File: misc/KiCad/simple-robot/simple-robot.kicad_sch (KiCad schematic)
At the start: 43 parts, among them J1 Conn_01x03_Pin, J2 Conn_01x03_Pin, J3 Conn_01x03_Pin, M1 Motor_DC, M2 Motor_DC, U1 Pico2

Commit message: schematic v2
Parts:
- added C9: 100nF_Ceramic, Capacitor_THT:C_Disc_D5.0mm_W2.5mm_P2.50mm, symbol PCM_SL_Capacitors:100nF_Ceramic
- added J4: Conn_01x03_Pin, Connector_PinHeader_2.54mm:PinHeader_1x03_P2.54mm_Vertical, symbol Connector:Conn_01x03_Pin
- added M3: Motor_Servo, symbol Motor:Motor_Servo
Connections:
- net GND: now also C9.2, J4.3 (Pin_3), M3.3 (-)
- net at C2.1, C5.2, C8.1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: now also C9.1, J4.2 (Pin_2), M3.2 (+)
- net at U1.7 (GPIO5): now also J4.1 (Pin_1), M3.1 (PWM)
- no-connect marks 17 -> 16

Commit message: update schematic and pcb
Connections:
- net at ENCB1.2 (Pin_2), EncoderB1.3 (PA), TP4.1 (Pin_1): now also U1.12 (GPIO9); no longer U1.11 (GPIO8)
- net at IMU1.8 (INT): now also U1.11 (GPIO8); no longer U1.12 (GPIO9)
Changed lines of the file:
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@@
+	(wire
+		(pts
+			(xy 78.74 124.46) (xy 83.82 124.46)
+		)
+		(stroke
+			(width 0)
+			(type default)
+		)
+	)
 	(wire
 		(pts
@@
 	(wire
 		(pts
-			(xy 73.66 55.88) (xy 73.66 124.46)
+			(xy 73.66 55.88) (xy 73.66 127)
 		)
 		(stroke
@@
 	(wire
 		(pts
-			(xy 78.74 162.56) (xy 78.74 127)
-		)
-		(stroke
-			(width 0)
-			(type default)
-		)
-	)
-	(wire
-		(pts
 			(xy 198.12 143.51) (xy 212.09 143.51)
 		)
@@
 	(wire
 		(pts
+			(xy 83.82 127) (xy 73.66 127)
+		)
+		(stroke
+			(width 0)
+			(type default)
+		)
+	)
+	(wire
+		(pts
 			(xy 130.81 139.7) (xy 119.38 139.7)
 		)
@@
 	(wire
 		(pts
+			(xy 78.74 124.46) (xy 78.74 162.56)
+		)
+		(stroke
+			(width 0)
+			(type default)
+		)
+	)
+	(wire
+		(pts
 			(xy 124.46 165.1) (xy 55.88 165.1)
 		)
@@
 	(wire
 		(pts
-			(xy 73.66 124.46) (xy 83.82 124.46)
-		)
-		(stroke
-			(width 0)
-			(type default)
-		)
-	)
-	(wire
-		(pts
 			(xy 77.47 30.48) (xy 118.11 30.48)
 		)
@@
 		)
 		(stroke
-			(width 0)
-			(type default)
-		)
-	)
-	(wire
-		(pts
-			(xy 78.74 127) (xy 83.82 127)
-		)
-		(stroke

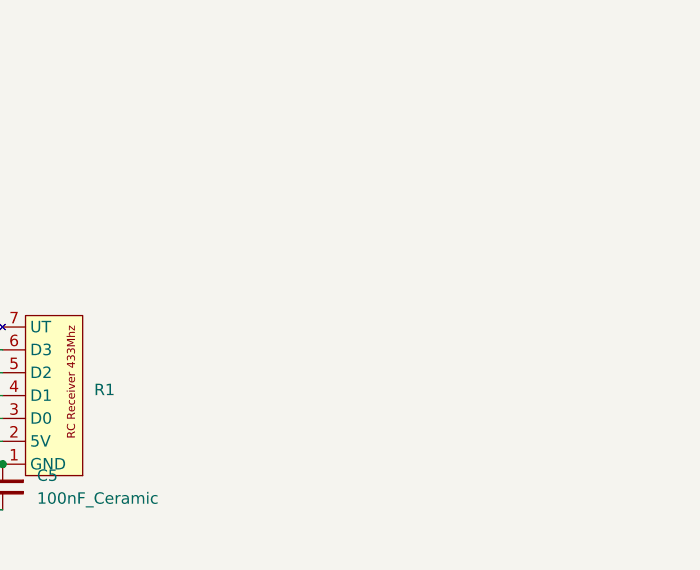
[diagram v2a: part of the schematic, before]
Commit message: update 3d models for hc-sr04 mount, update KiCad files, update schematic and PCB
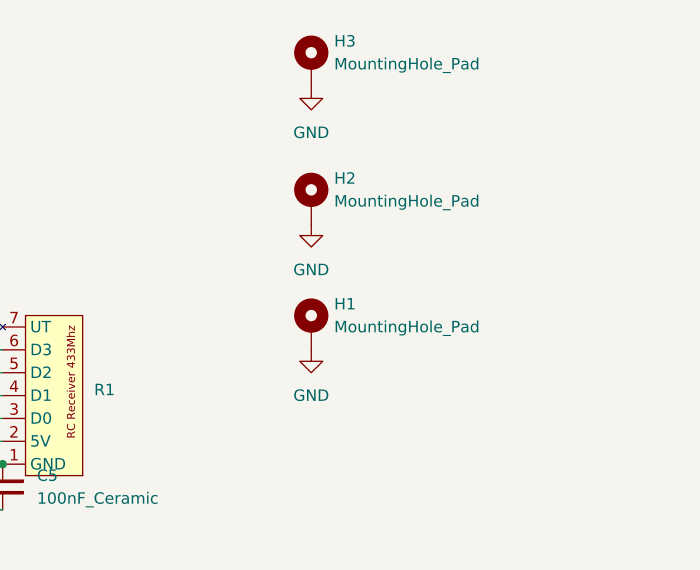
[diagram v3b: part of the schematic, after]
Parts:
- added H1, H2, H3: MountingHole_Pad, MountingHole:MountingHole_3.7mm_Pad_Via, symbol Mechanical:MountingHole_Pad
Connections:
- net GND: now also H1.1, H2.1, H3.1

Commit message: debugging & rewire
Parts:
- removed C2, C3: 47uF_25V, Capacitor_THT:CP_Radial_D5.0mm_P2.00mm, symbol PCM_SL_Capacitors:47uF_25V
- removed C7: 100nF_Ceramic, Capacitor_THT:C_Disc_D5.0mm_W2.5mm_P2.50mm, symbol PCM_SL_Capacitors:100nF_Ceramic
- removed D1, D2: 1N5817, Diode_THT:D_DO-41_SOD81_P10.16mm_Horizontal, symbol Diode:1N5817
- removed R4: 10k, Resistor_THT:R_Axial_DIN0207_L6.3mm_D2.5mm_P10.16mm_Horizontal, symbol PCM_SL_Resistors:10k
- removed R5: 20k, Resistor_THT:R_Axial_DIN0207_L6.3mm_D2.5mm_P10.16mm_Horizontal, symbol PCM_SL_Resistors:20k
- added C10, C11, C12, C13, C14, C15, C3: 100nF_Ceramic, Capacitor_THT:C_Disc_D5.0mm_W2.5mm_P2.50mm, symbol PCM_SL_Capacitors:100nF_Ceramic
- added C17, C2: 220uF_10V, Capacitor_THT:CP_Radial_D6.3mm_P2.50mm, symbol PCM_SL_Capacitors:220uF_10V
- added LS_2: ~, common-hobby-things:Level shifter 4 bi-dir, symbol common-hobby-things:level-shifter
- added TPGND1, TPGND2: Conn_01x01_Pin, symbol Connector:Conn_01x01_Pin
- renumbered J2 to DBG1, J3 to IRL1, J1 to IRR1, IR_Proximity_Sensor2 to IR_Sensor_Left1, IR_Proximity_Sensor1 to IR_Sensor_Right1, M1 to MA1, M2 to MB1, J4 to SERVO1, TP3 to TPENCA1, TP4 to TPENCB1, TP1 to TPSCL1, TP2 to TPSDA1
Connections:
- net GND: now also C4.2, C5.2, U1.13 (GND), U1.28 (GND), U1.8 (GND), C10.2, C11.1, C12.1, C13.2, C14.2, C15.2, C17.2, C2.2, C3.2, LS_2.10 (GND), LS_2.4 (GND), TPGND1.1 (Pin_1), TPGND2.1 (Pin_1); no longer C4.1, C5.1, U1.42 (GND)
- net at ENCB1.2 (Pin_2), EncoderB1.3 (PA), TPENCB1.1 (Pin_1): now also LS_2.7 (HV1); no longer U1.12 (GPIO9)
- net at C6.2, IMU1.1 (VCC), IRL1.2 (Pin_2)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: now also C4.1, C8.1, C14.1, C15.1, LS_2.3 (LV); no longer C4.2
- net at IRL1.1 (Pin_1), IR_Sensor_Left1.3 (OUT): now also U1.9 (GPIO6)
- net at C9.1, ENCA1.3 (Pin_3), ENCB1.3 (Pin_3)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: now also C5.1, C10.1, C11.2, C12.2, C13.1, C17.1, C3.1, LS_2.9 (HV); no longer C5.2, C8.1
- net at C1.1, MD1.7 (VMOT), S6V1.3 (VOUT): now also C2.1
- net at U1.31 (GPIO26_ADC0): now also IRR1.1 (Pin_1), IR_Sensor_Right1.3 (OUT)
- net at U1.19 (GPIO14): now also LS_2.5 (LV3)
- net at MD1.3 (A01), MOTA1.1 (Pin_1): now also MA1.1 (+); no longer MB1.1 (+)
- net at MD1.4 (A02), MOTA1.2 (Pin_2): now also MA1.2 (-); no longer MB1.2 (-)
- net at R1.3 (D0): now also LS_1.12 (HV4); no longer LS_1.7 (HV1)
- net at R1.4 (D1): now also LS_1.11 (HV3); no longer LS_1.8 (HV2)
- net at R1.5 (D2): now also LS_1.8 (HV2); no longer LS_1.11 (HV3)
- net at R1.6 (D3): now also LS_1.7 (HV1); no longer LS_1.12 (HV4)
- net at ENCA1.2 (Pin_2), EncoderA1.3 (PA), TPENCA1.1 (Pin_1): now also LS_2.8 (HV2); no longer U1.10 (GPIO7)
- net at LS_1.5 (LV3): now also U1.21 (GPIO16); no longer U1.14 (GPIO10)
- net at U1.15 (GPIO11): now also LS_1.2 (LV2); no longer LS_1.6 (LV4)
- net at HC-SR04-1.2 (TRIG), HC-SRo4.2 (Pin_2): now also LS_2.12 (HV4); no longer U1.20 (GPIO15)
- net at LS_1.1 (LV1): now also U1.22 (GPIO17); no longer U1.21 (GPIO16)
- net at HC-SR04-1.3 (ECHO), HC-SRo4.3 (Pin_3): now also LS_2.11 (HV3)
- new net: MB1.2 (-), MD1.5 (B02), MOTB1.2 (Pin_2)
- new net: MB1.1 (+), MD1.6 (B01), MOTB1.1 (Pin_1)
- new net: LS_2.1 (LV1), U1.12 (GPIO9)
- new net: LS_2.2 (LV2), U1.10 (GPIO7)
- new net: LS_2.6 (LV4), U1.20 (GPIO15)
- new net: LS_1.6 (LV4), U1.14 (GPIO10)
- no-connect marks 16 -> 13
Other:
- moved on the sheet: BATT1, C1, C4, C5, C6, C9, D3, DBG1, ENCA1, ENCB1, EncoderA1, EncoderB1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

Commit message: Update KiCad project files and remove unnecessary autosave and lock files
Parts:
- TPGND1, TPGND2: footprint (none) -> Connector_PinHeader_2.54mm:PinHeader_1x01_P2.54mm_Vertical
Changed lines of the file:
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@@
 			)
 		)
-		(property "Footprint" ""
+		(property "Footprint" "Connector_PinHeader_2.54mm:PinHeader_1x01_P2.54mm_Vertical"
 			(at 267.97 92.71 0)
 			(effects
@@
 			)
 		)
-		(property "Footprint" ""
+		(property "Footprint" "Connector_PinHeader_2.54mm:PinHeader_1x01_P2.54mm_Vertical"
 			(at 267.97 82.55 0)
 			(effects

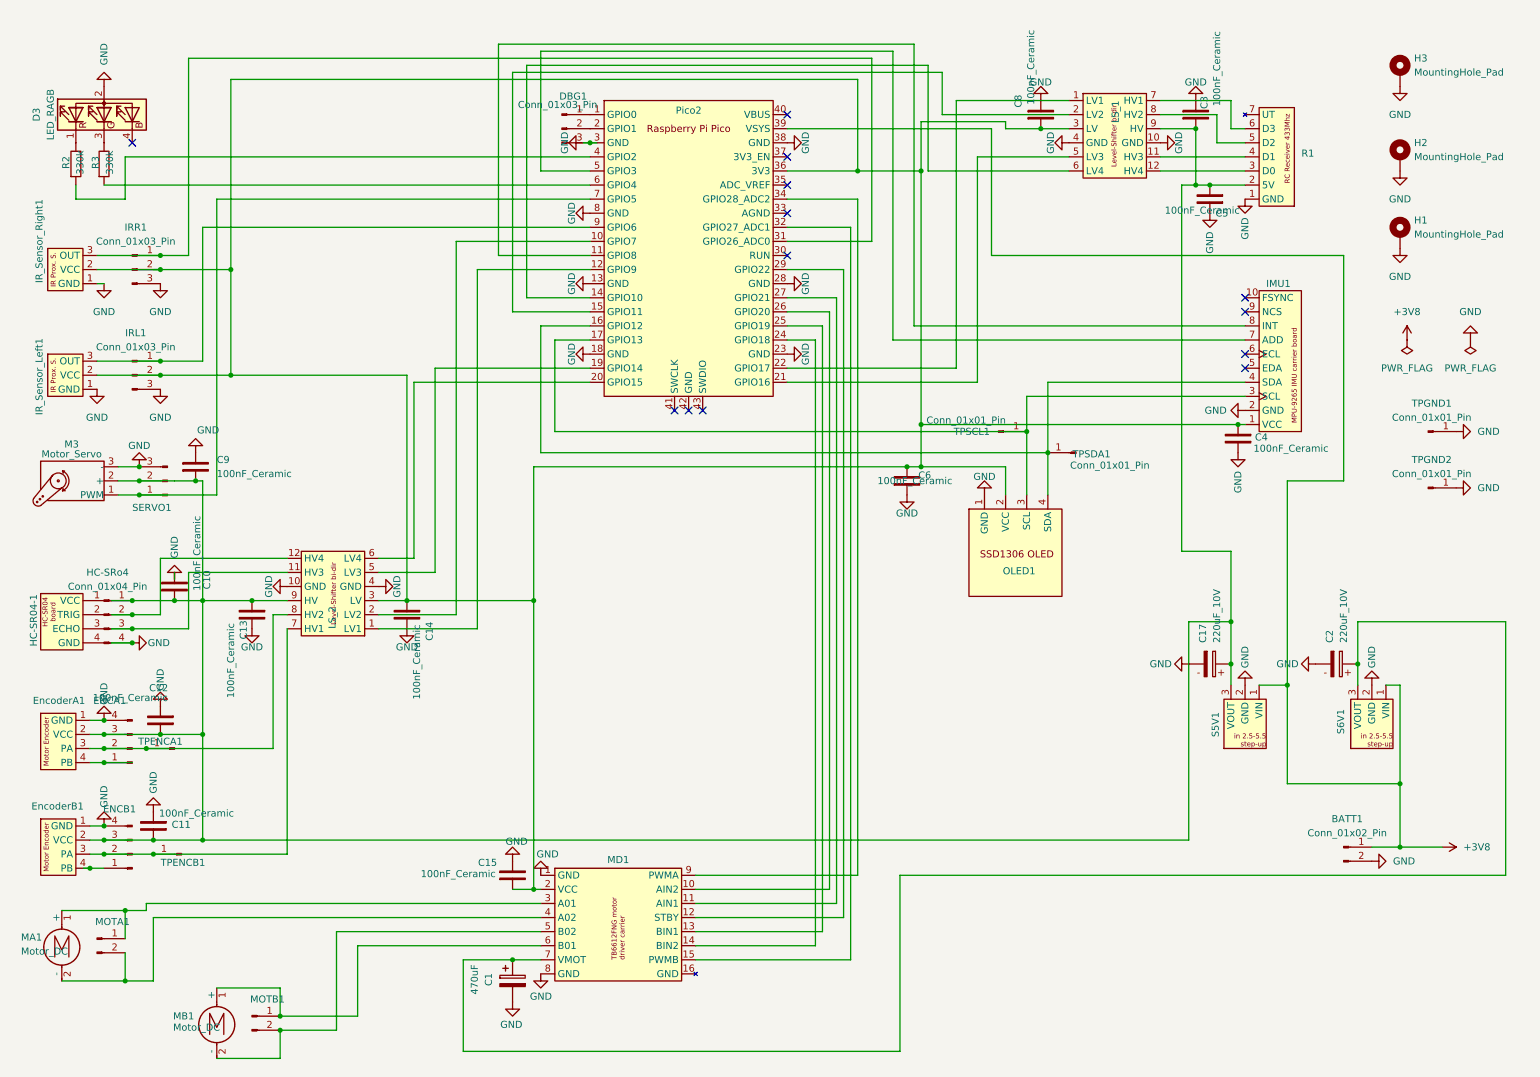
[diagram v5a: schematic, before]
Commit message: Dev into main (#18)
* Port expander and pin redistribution (#11)

* isolate few components to start with, comment the rest. Introduce new
motor driver without tb6612fng driver, also use a new port expander for
this.

* Add flash-backed calibration storage

Add sequential-storage and embedded-storage-async dependencies and use
the async Flash API. Reserve the last 8KB of flash in memory.x and
expose a FLASH_STORAGE region. Add src/task/flash_storage.rs which
implements a flash storage task, commands, and serialization for motor
and IMU calibration data. Remove the encoder_read task and update task
module, motor_driver docs, and main imports accordingly

* Include dev branch in CI workflow

* Fix PR review comments: correct type usage, add div-by-zero protection, fix memory.x comment

- Fixed incorrect type imports in drive.rs: use Track and Motor instead of MotorDriver and MotorSelection
- Updated all motor control calls to use correct Track enum (Left/Right) instead of incorrectly using Left for both sides
- Simplified MotorState methods to use SetTrack commands for controlling entire tracks
- Added division by zero protection in motor calibration routine (3 locations)
- Fixed memory.x comment to correctly state 8KB (two 4KB sectors) allocation
- Updated CI workflow to include dev branch for push and PR triggers

* Group crate::task imports and fix ordering

* Fix clippy warnings for CI

- Rename FlashCommand variants to remove common 'Calibration' postfix
- Derive Default for CalibrationData instead of manual impl
- Use unsigned_abs() instead of abs() as u8 cast
- Rename PortExpanderCommand variants to remove common 'Set' prefix
- Collapse nested if statements for button state checking
- Use is_err() instead of redundant pattern matching
- Update all usage sites and documentation to match renamed variants

* Drive straight (#12)

* Refactor flash storage and init wiring

Use Signal to return motor and IMU calibration data and add
CalibrationKind/CalibrationDataKind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
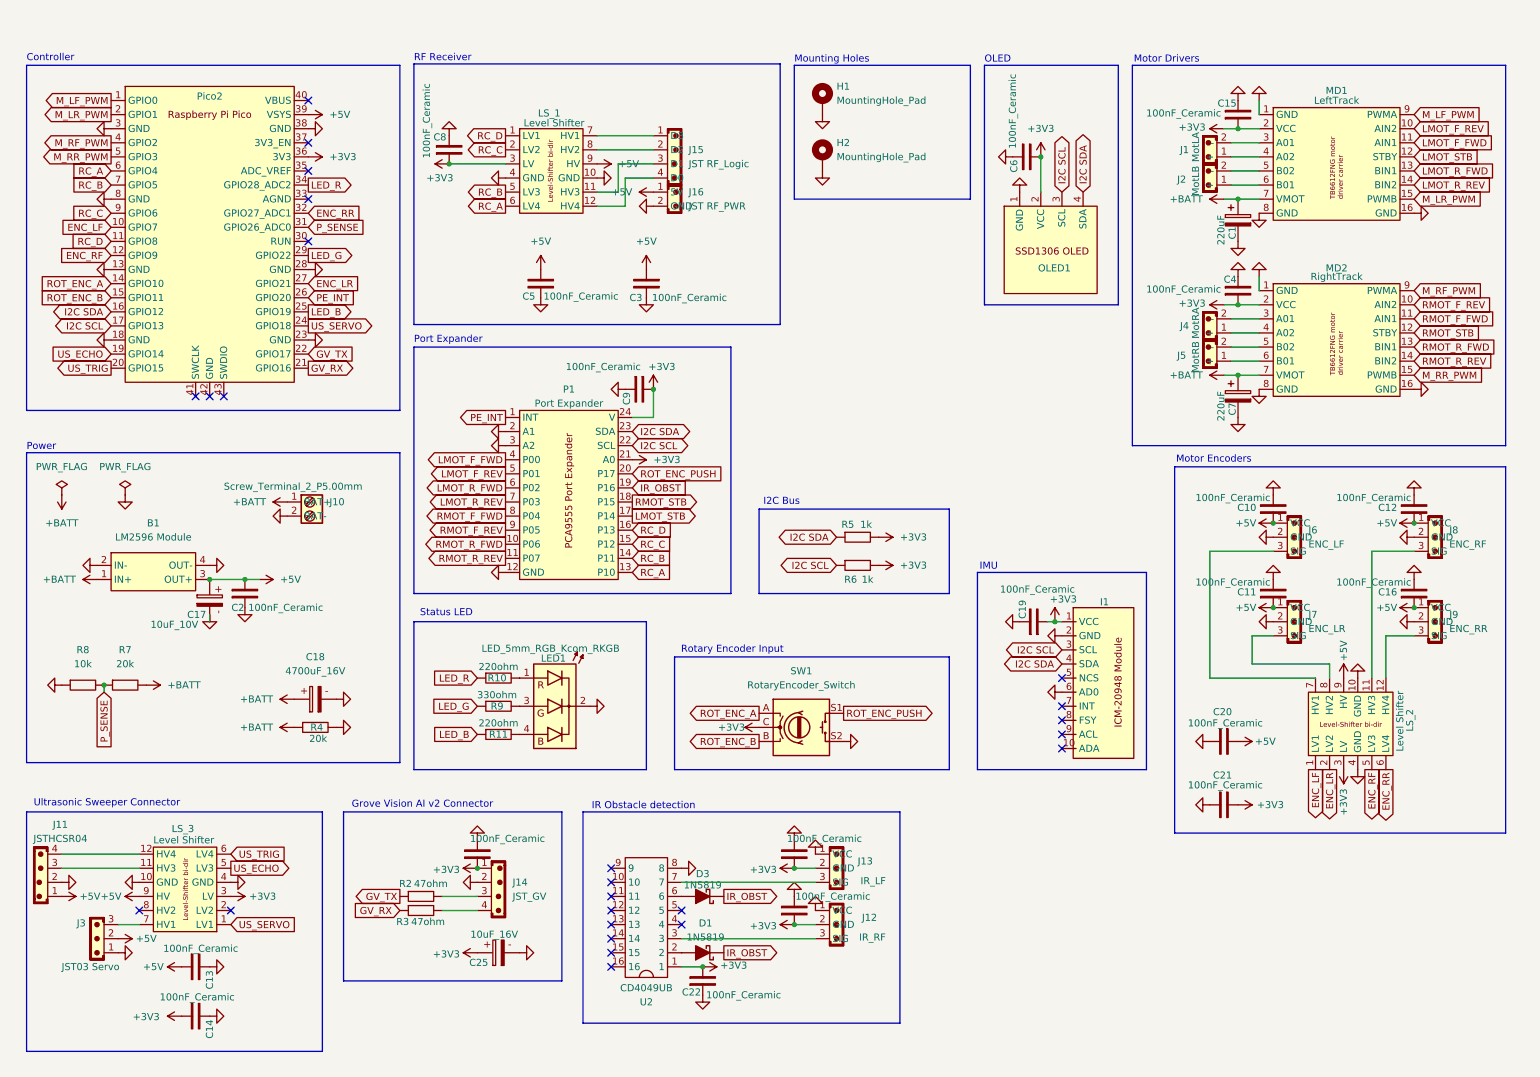
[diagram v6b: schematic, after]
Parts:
- removed BATT1: Conn_01x02_Pin, Connector_PinHeader_2.54mm:PinHeader_1x02_P2.54mm_Vertical, symbol Connector:Conn_01x02_Pin
- removed C2: 220uF_10V, Capacitor_THT:CP_Radial_D6.3mm_P2.50mm, symbol PCM_SL_Capacitors:220uF_10V
- removed D3: LED_RAGB, common-hobby-things:LED RAGB, symbol Device:LED_RAGB
- removed DBG1, IRL1, IRR1, SERVO1: Conn_01x03_Pin, Connector_PinHeader_2.54mm:PinHeader_1x03_P2.54mm_Vertical, symbol Connector:Conn_01x03_Pin
- removed ENCA1, ENCB1, HC-SRo4: Conn_01x04_Pin, Connector_PinHeader_2.54mm:PinHeader_1x04_P2.54mm_Vertical, symbol Connector:Conn_01x04_Pin
- removed EncoderA1, EncoderB1: ~, symbol common-hobby-things:Hall-effect_encoder
- removed H3: MountingHole_Pad, MountingHole:MountingHole_3.7mm_Pad_Via, symbol Mechanical:MountingHole_Pad
- removed HC-SR04-1: ~, symbol common-hobby-things:HC-SR04
- removed IMU1: ~, common-hobby-things:MPU 9265 IMU carrier board, symbol common-hobby-things:GY-9250_9-Axis
- removed IR_Sensor_Left1, IR_Sensor_Right1: ~, symbol common-hobby-things:IR_Proximity_Sensor
- removed M3: Motor_Servo, symbol Motor:Motor_Servo
- removed MA1, MB1: Motor_DC, symbol Motor:Motor_DC
- removed MOTA1, MOTB1: ~, Connector_PinHeader_2.54mm:PinHeader_1x02_P2.54mm_Vertical, symbol Connector:Conn_01x02_Pin
- removed R1: ~, common-hobby-things:433Mhz RC Receiver, symbol common-hobby-things:RC_Receiver
- removed R2, R3: 330k, Resistor_THT:R_Axial_DIN0207_L6.3mm_D2.5mm_P10.16mm_Horizontal, symbol PCM_SL_Resistors:330k
- removed S5V1: ~, common-hobby-things:Pololu step-up converter 2.5-5.5V in 5V out, symbol common-hobby-things:step-up-converter_5V
- removed S6V1: ~, common-hobby-things:Pololu step-up converter 2.5-5.5V in 6V out, symbol common-hobby-things:step-up-converter_6V
- removed TPENCA1, TPENCB1, TPGND1, TPGND2, TPSCL1, TPSDA1: Conn_01x01_Pin, Connector_PinHeader_2.54mm:PinHeader_1x01_P2.54mm_Vertical, symbol Connector:Conn_01x01_Pin
- added B1: LM2596 Module, common-hobby-things:LM2596_Module, symbol common-hobby-things:LM2596_Module
- added C16, C19, C2, C20, C21, C22, C23, C24, C26: 100nF_Ceramic, Capacitor_THT:C_Disc_D5.0mm_W2.5mm_P2.50mm, symbol PCM_SL_Capacitors:100nF_Ceramic
- added C18: 4700uF_16V, Capacitor_THT:CP_Radial_D16.0mm_P7.50mm, symbol PCM_SL_Capacitors:4700uF_16V
- added C25: 10uF_16V, Capacitor_THT:CP_Radial_D5.0mm_P2.00mm, symbol PCM_SL_Capacitors:10uF_16V
- added C7: 220uF, Capacitor_THT:CP_Radial_D6.3mm_P2.50mm, symbol Device:C_Polarized
- added D1, D3: 1N5819, PCM_Diode_THT_AKL:D_DO-41_SOD81_P7.62mm_Horizontal, symbol PCM_Diode_Schottky_AKL:1N5819
- added I1: ~, common-hobby-things:ICM-20948-module, symbol common-hobby-things:ICM-20948-module
- added J1: MotLA, Connector_JST:JST_PH_B2B-PH-K_1x02_P2.00mm_Vertical, symbol PCM_SL_Connectors:JST_02
- added J10: Screw_Terminal_2_P5.00mm, TerminalBlock_Phoenix:TerminalBlock_Phoenix_PT-1,5-2-5.0-H_1x02_P5.00mm_Horizontal, symbol PCM_SL_Screw_Terminal:Screw_Terminal_2_P5.00mm
- added J11: JSTHCSR04, Connector_JST:JST_EH_B4B-EH-A_1x04_P2.50mm_Vertical, symbol PCM_SL_Connectors:JST_04
- added J12: IR_RF, Connector_JST:JST_PH_B3B-PH-K_1x03_P2.00mm_Vertical, symbol PCM_SL_Connectors:JST_03
- added J13: IR_LF, Connector_JST:JST_PH_B3B-PH-K_1x03_P2.00mm_Vertical, symbol PCM_SL_Connectors:JST_03
- added J14: JST_GV, Connector_JST:JST_EH_B4B-EH-A_1x04_P2.50mm_Vertical, symbol PCM_SL_Connectors:JST_04
- added J15: JST RF_Logic, Connector_JST:JST_EH_B4B-EH-A_1x04_P2.50mm_Vertical, symbol PCM_SL_Connectors:JST_04
- added J16: JST RF_PWR, Connector_JST:JST_EH_B2B-EH-A_1x02_P2.50mm_Vertical, symbol PCM_SL_Connectors:JST_02
- added J2: MotLB, Connector_JST:JST_PH_B2B-PH-K_1x02_P2.00mm_Vertical, symbol PCM_SL_Connectors:JST_02
- added J3: JST03 Servo, Connector_JST:JST_EH_B3B-EH-A_1x03_P2.50mm_Vertical, symbol PCM_SL_Connectors:JST_03
- added J4: MotRA, Connector_JST:JST_PH_B2B-PH-K_1x02_P2.00mm_Vertical, symbol PCM_SL_Connectors:JST_02
- added J5: MotRB, Connector_JST:JST_PH_B2B-PH-K_1x02_P2.00mm_Vertical, symbol PCM_SL_Connectors:JST_02
- added J6: ENC_LF, Connector_JST:JST_PH_B3B-PH-K_1x03_P2.00mm_Vertical, symbol PCM_SL_Connectors:JST_03
- added J7: ENC_LR, Connector_JST:JST_PH_B3B-PH-K_1x03_P2.00mm_Vertical, symbol PCM_SL_Connectors:JST_03
- added J8: ENC_RF, Connector_JST:JST_PH_B3B-PH-K_1x03_P2.00mm_Vertical, symbol PCM_SL_Connectors:JST_03
- added J9: ENC_RR, Connector_JST:JST_PH_B3B-PH-K_1x03_P2.00mm_Vertical, symbol PCM_SL_Connectors:JST_03
- added LED1: LED_5mm_RGB_Kcom_RKGB, PCM_LED_THT_AKL:LED_D5.0mm-4_RGB_Wide_Pins, symbol PCM_LED_AKL:LED_5mm_RGB_Kcom_RKGB
- added LS_3: Level Shifter, common-hobby-things:Level shifter 4 bi-dir, symbol common-hobby-things:level-shifter
- added MD2: RightTrack, common-hobby-things:TB6612FNG motor driver carrier, symbol common-hobby-things:TB6612FNG motor driver carrier
- added P1: Port Expander, common-hobby-things:PCA9555 Port Expander, symbol common-hobby-things:PCA9555
- added R10, R11: 220ohm, Resistor_THT:R_Axial_DIN0207_L6.3mm_D2.5mm_P10.16mm_Horizontal, symbol PCM_SL_Resistors:220ohm
- added R2, R3: 47ohm, Resistor_THT:R_Axial_DIN0207_L6.3mm_D2.5mm_P10.16mm_Horizontal, symbol PCM_SL_Resistors:47ohm
- added R4, R7: 20k, Resistor_THT:R_Axial_DIN0207_L6.3mm_D2.5mm_P10.16mm_Horizontal, symbol PCM_SL_Resistors:20k
- added R5, R6: 1k, Resistor_THT:R_Axial_DIN0207_L6.3mm_D2.5mm_P10.16mm_Horizontal, symbol PCM_SL_Resistors:1k
- added R8: 10k, Resistor_THT:R_Axial_DIN0207_L6.3mm_D2.5mm_P10.16mm_Horizontal, symbol PCM_SL_Resistors:10k
- added R9: 330ohm, Resistor_THT:R_Axial_DIN0207_L6.3mm_D2.5mm_P10.16mm_Horizontal, symbol PCM_SL_Resistors:330ohm
- added SW1: RotaryEncoder_Switch, Rotary_Encoder:RotaryEncoder_Alps_EC11E-Switch_Vertical_H20mm, symbol Device:RotaryEncoder_Switch
- added U2: CD4049UB, Package_DIP:DIP-16_W7.62mm_LongPads, symbol PCM_SL_Devices:IC_DIP_16
- C1: value 470uF -> 220uF
- C17: value 220uF_10V -> 10uF_10V
- LS_1, LS_2: value ~ -> Level Shifter
- MD1: value ~ -> LeftTrack
- U1: footprint MCU_RaspberryPi_and_Boards:RPi_Pico_SMD_TH -> PCM_SL_Development_Boards:raspberry_pi_pico_THT
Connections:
- net +3V8 is gone; now on net +5V: U1.39 (VSYS)
- net GND: now also C11.2, C12.2, C9.1, MD1.16 (GND), B1.2 (IN-), B1.4 (OUT-), C16.2, C18.2, C19.2, C2.1, C20.1, C21.1, C22.1, C23.2, C24.2, C25.2, C26.2, C7.2, I1.2 (GND), I1.6 (AD0), J10.2 (BAT-), J11.2, J12.1 (VCC), J13.1 (VCC), J14.2, J16.2 (GND), J3.1, J6.2 (GND), J7.2 (GND), J8.2 (GND), J9.2 (GND), LED1.2 (A), LS_3.10 (GND), LS_3.4 (GND), MD2.1 (GND), MD2.16 (GND), MD2.8 (GND), P1.12 (GND), P1.2 (A1), P1.3 (A2), R4.2, R8.1, SW1.S2, U2.8; no longer C11.1, C12.1, C9.2
- net at LS_2.7 (HV1): now also J6.3 (SIG)
- net +3V3: now reaches C14.1, C15.1, C4.1, C6.2, C8.1, LS_1.3 (LV), LS_2.3 (LV), MD1.2 (VCC), OLED1.2 (VCC), U1.36 (3V3)
- net +3V3: now also C9.2, C19.1, C21.2, C22.2, C23.1, C24.1, C25.1, C26.1, I1.1 (VCC), J12.2 (GND), J13.2 (GND), J14.1, LS_3.3 (LV), MD2.2 (VCC), P1.21 (A0), P1.24 (V), R5.2, R6.2, SW1.C, U2.1
- net RC_C: now reaches U1.9 (GPIO6)
- net RC_C: now also LS_1.2 (LV2), P1.15 (P12)
- net +5V: now reaches C10.1, C13.1, C17.1, C3.1, C5.1, LS_1.9 (HV), LS_2.9 (HV)
- net +5V: now also C11.1, C12.1, B1.3 (OUT+), C16.1, C2.2, C20.2, J11.1, J16.1 (5V), J3.2, J6.1 (VCC), J7.1 (VCC), J8.1 (VCC), J9.1 (VCC), LS_3.9 (HV); no longer C11.2, C12.2, C9.1
- net RC_B: now reaches U1.7 (GPIO5)
- net RC_B: now also LS_1.5 (LV3), P1.14 (P11)
- net M_RF_PWM: now reaches U1.4 (GPIO2)
- net M_RF_PWM: now also MD2.9 (PWMA)
- net I2C SDA: now reaches OLED1.4 (SDA), U1.16 (GPIO12)
- net I2C SDA: now also I1.4 (SDA), P1.23 (SDA), R5.1
- net +BATT: now reaches C1.1, MD1.7 (VMOT)
- net +BATT: now also B1.1 (IN+), C18.1, C7.1, J10.1 (BAT+), MD2.7 (VMOT), R4.1, R7.2
- net P_SENSE: now reaches U1.31 (GPIO26_ADC0)
- net P_SENSE: now also R7.1, R8.2
- net at MD1.3 (A01): now also J1.2 (-)
- net at MD1.4 (A02): now also J1.1 (+)
- net M_LF_PWM: now reaches U1.1 (GPIO0)
- net M_LF_PWM: now also MD1.9 (PWMA)
- net M_LR_PWM: now reaches U1.2 (GPIO1)
- net M_LR_PWM: now also MD1.15 (PWMB)
- net RC_A: now reaches U1.6 (GPIO4)
- net RC_A: now also LS_1.6 (LV4), P1.13 (P10)
- net LMOT_F_REV: now reaches MD1.10 (AIN2)
- net LMOT_F_REV: now also P1.5 (P01); no longer U1.26 (GPIO20)
- net ENC_LR: now reaches U1.27 (GPIO21)
- net ENC_LR: now also LS_2.2 (LV2); no longer MD1.11 (AIN1)
- net LED_G: now reaches U1.29 (GPIO22)
- net LED_G: now also R9.1; no longer MD1.12 (STBY)
- net LED_B: now reaches U1.25 (GPIO19)
- net LED_B: now also R11.1; no longer MD1.13 (BIN1)
- net LMOT_R_REV: now reaches MD1.14 (BIN2)
- net LMOT_R_REV: now also P1.7 (P03); no longer U1.24 (GPIO18)
- net ENC_RR: now reaches U1.32 (GPIO27_ADC1)
- net ENC_RR: now also LS_2.6 (LV4); no longer MD1.15 (PWMB)
- net at MD1.5 (B02): now also J2.2 (-)
- net at MD1.6 (B01): now also J2.1 (+)
- net LED_R: now reaches U1.34 (GPIO28_ADC2)
- net LED_R: now also R10.1; no longer MD1.9 (PWMA)
- net at LS_1.12 (HV4): now also J15.4 (D0)
- net at LS_1.11 (HV3): now also J15.3 (D1)
- net at LS_1.8 (HV2): now also J15.2 (D2)
- net at LS_1.7 (HV1): now also J15.1 (D3)
- net at LS_2.8 (HV2): now also J7.3 (SIG)
- net ENC_LF: now reaches LS_2.1 (LV1)
- net ENC_LF: now also U1.10 (GPIO7); no longer U1.12 (GPIO9)
- net at LS_2.11 (HV3): now also J8.3 (SIG)
- net at LS_2.12 (HV4): now also J9.3 (SIG)
- net ENC_RF: now reaches LS_2.5 (LV3)
- net ENC_RF: now also U1.12 (GPIO9); no longer U1.19 (GPIO14)
- net US_TRIG: now reaches U1.20 (GPIO15)
- net US_TRIG: now also LS_3.6 (LV4); no longer LS_2.6 (LV4)
- net I2C SCL: now reaches OLED1.3 (SCL), U1.17 (GPIO13)
- net I2C SCL: now also I1.3 (SCL), P1.22 (SCL), R6.1
- net GV_TX: now reaches U1.22 (GPIO17)
- net GV_TX: now also R2.1; no longer LS_1.1 (LV1)
- net ROT_ENC_B: now reaches U1.15 (GPIO11)
- net ROT_ENC_B: now also SW1.B; no longer LS_1.2 (LV2)
- net GV_RX: now reaches U1.21 (GPIO16)
- net GV_RX: now also R3.1; no longer LS_1.5 (LV3)
- net ROT_ENC_A: now reaches U1.14 (GPIO10)
- net ROT_ENC_A: now also SW1.A; no longer LS_1.6 (LV4)
- net RC_D: now reaches U1.11 (GPIO8)
- net RC_D: now also LS_1.1 (LV1), P1.16 (P13)
- net M_RR_PWM: now reaches U1.5 (GPIO3)
- net M_RR_PWM: now also MD2.15 (PWMB)
- new net: J14.3, R2.2
- new net: J14.4, R3.2
- new net: D1.2 (A), U2.2
- new net: J12.3 (SIG), U2.3
- new net: D3.2 (A), U2.6
- new net: J13.3 (SIG), U2.7
- new net: J11.3, LS_3.11 (HV3)
- new net: J11.4, LS_3.12 (HV4)
- new net: J4.1 (+), MD2.4 (A02)
- new net: J4.2 (-), MD2.3 (A01)
- new net: J3.3, LS_3.7 (HV1)
- new net: LED1.3 (G), R9.2
- new net: LED1.1 (R), R10.2
- new net: LED1.4 (B), R11.2
- new net: J5.2 (-), MD2.5 (B02)
- new net: J5.1 (+), MD2.6 (B01)
- new net IR_OBST: D1.1 (K), D3.1 (K), P1.19 (P16)
- new net LMOT_F_FWD: MD1.11 (AIN1), P1.4 (P00)
- new net LMOT_R_FWD: MD1.13 (BIN1), P1.6 (P02)
- new net LMOT_STB: MD1.12 (STBY), P1.17 (P14)
- new net PE_INT: P1.1 (INT), U1.26 (GPIO20)
- new net RMOT_F_FWD: MD2.11 (AIN1), P1.8 (P04)
- new net RMOT_F_REV: MD2.10 (AIN2), P1.9 (P05)
- new net RMOT_R_FWD: MD2.13 (BIN1), P1.10 (P06)
- new net RMOT_R_REV: MD2.14 (BIN2), P1.11 (P07)
- new net RMOT_STB: MD2.12 (STBY), P1.18 (P15)
- new net ROT_ENC_PUSH: P1.20 (P17), SW1.S1
- new net US_ECHO: LS_3.5 (LV3), U1.19 (GPIO14)
- new net US_SERVO: LS_3.1 (LV1), U1.24 (GPIO18)
- no-connect marks 13 -> 25
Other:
- note added: "Controller"
- note added: "Grove Vision AI v2 Connector"
- note added: "I2C Bus"
- note added: "IMU"
- note added: "IR Obstacle detection"
- note added: "Motor Drivers"
- note added: "Motor Encoders"
- note added: "Mounting Holes"
- note added: "OLED"
- note added: "Port Expander"
- note added: "Power"
- note added: "RF Receiver"
- note added: "Rotary Encoder Input"
- note added: "Status LED"
- note added: "Ultrasonic Sweeper Connector"
- moved on the sheet: C1, C13, C14, C15, C17, C3, C5, C6, C8, H1, H2, LS_1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
